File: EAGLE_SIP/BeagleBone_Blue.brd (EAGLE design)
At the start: 86.4 x 54.6 mm, 202 parts, among them J1 USD_CONNECTOR, M1 JST_ZH_2, M2 JST_ZH_2, M3 JST_ZH_2, M4 JST_ZH_2, Q3 MOSFET-N, U5 24LC_32AT-I/OT, U6 SN74LVC1G07_DCK_5, Y1 CM200C-32.768KAZF-UT, Y2 445C33D24M00000

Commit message: Small shifts
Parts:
- moved TP5 10.2 mm to (32.0, -25.1)
- moved RESET 0.15 mm to (5.17, -15.4)
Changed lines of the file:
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@@
 </element>
 <element name="RED" library="SparkFun-LED" package="LED-0603" value="RED" x="44.9199" y="-52.7939"/>
-<element name="RESET" library="SparkFun-Electromechanical" package="TACTILE-SWITCH-1101NE" value="SWITCH-MOMENTARY-2SMD-1101NE" x="5.3213" y="-15.4178" smashed="yes">
-<attribute name="PROD_ID" value="SWCH-00815" x="5.3213" y="-15.4178" size="1.778" layer="27" display="off"/>
-<attribute name="NAME" x="9.8778" y="-15.8689" size="1.27" layer="25"/>
+<element name="RESET" library="SparkFun-Electromechanical" package="TACTILE-SWITCH-1101NE" value="SWITCH-MOMENTARY-2SMD-1101NE" x="5.1689" y="-15.4178" smashed="yes">
+<attribute name="PROD_ID" value="SWCH-00815" x="5.1689" y="-15.4178" size="1.778" layer="27" display="off"/>
+<attribute name="NAME" x="9.7254" y="-15.8689" size="1.27" layer="25"/>
 </element>
 <element name="SIP" library="BeagleBone_Blue" package="OSD3358" value="OSD3358" x="46.6725" y="-36.9316" rot="MR270"/>
@@
 <attribute name="TP_SIGNAL_NAME" value="" x="65.4939" y="-11.7348" size="1.778" layer="28" rot="MR0" display="off"/>
 </element>
-<element name="TP5" library="testpad" package="B1,27" value="TPSQB1,27" x="31.8516" y="-14.9352" rot="MR0">
-<attribute name="TP_SIGNAL_NAME" value="" x="31.8516" y="-14.9352" size="1.778" layer="28" rot="MR0" display="off"/>
+<element name="TP5" library="testpad" package="B1,27" value="TPSQB1,27" x="32.004" y="-25.146" rot="MR0">
+<attribute name="TP_SIGNAL_NAME" value="" x="32.004" y="-25.146" size="1.778" layer="28" rot="MR0" display="off"/>
 </element>
 <element name="TP7" library="testpad" package="B1,27" value="TPSQB1,27" x="45.085" y="-51.0032" rot="MR180">
@@
 <wire x1="5.0391" y1="-5.334" x2="8.0391" y2="-10.134" width="0" layer="19" extent="1-1"/>
 <wire x1="2.0447" y1="-13.6784" x2="8.0391" y2="-10.134" width="0" layer="19" extent="16-16"/>
-<wire x1="2.1713" y1="-15.4178" x2="2.0447" y2="-13.6784" width="0" layer="19" extent="1-16"/>
-<wire x1="2.0447" y1="-16.4284" x2="2.1713" y2="-15.4178" width="0" layer="19" extent="1-16"/>
+<wire x1="2.0189" y1="-15.4178" x2="2.0447" y2="-13.6784" width="0" layer="19" extent="1-16"/>
+<wire x1="2.0447" y1="-16.4284" x2="2.0189" y2="-15.4178" width="0" layer="19" extent="1-16"/>
 <wire x1="2.0447" y1="-18.9284" x2="2.0447" y2="-16.4284" width="0" layer="19" extent="16-16"/>
 <wire x1="2.0189" y1="-20.5994" x2="2.0447" y2="-18.9284" width="0" layer="19" extent="1-16"/>
@@
 <wire x1="34.671" y1="-12.4079" x2="37.6809" y2="-9.4742" width="0" layer="19" extent="1-1"/>
 <wire x1="21.4353125" y1="-18.3134" x2="34.671" y2="-12.4079" width="0" layer="19" extent="1-1"/>
-<wire x1="8.4713" y1="-15.4178" x2="21.4353125" y2="-18.3134" width="0" layer="19" extent="1-1"/>
+<wire x1="8.3189" y1="-15.4178" x2="21.4353125" y2="-18.3134" width="0" layer="19" extent="1-1"/>
 <wire x1="47.3075" y1="-24.8666" x2="34.671" y2="-12.4079" width="0" layer="19" extent="1-16"/>
 </signal>
@@
 <contactref element="TP5" pad="TP"/>
 <wire x1="35.8775" y1="-28.6766" x2="52.3875" y2="-27.4066" width="0" layer="19" extent="16-16"/>
-<wire x1="31.8516" y1="-14.9352" x2="35.8775" y2="-28.6766" width="0" layer="19" extent="16-16"/>
+<wire x1="32.004" y1="-25.146" x2="35.8775" y2="-28.6766" width="0" layer="19" extent="16-16"/>
 </signal>
 <signal name="I2C0_SCL">

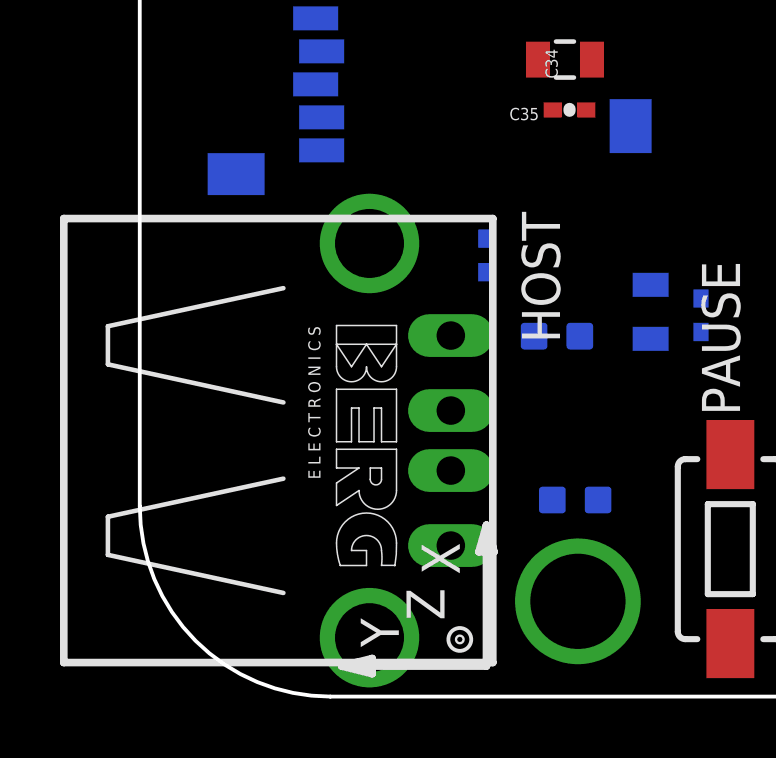
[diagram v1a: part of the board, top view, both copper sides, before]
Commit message: Small shifts for DRC
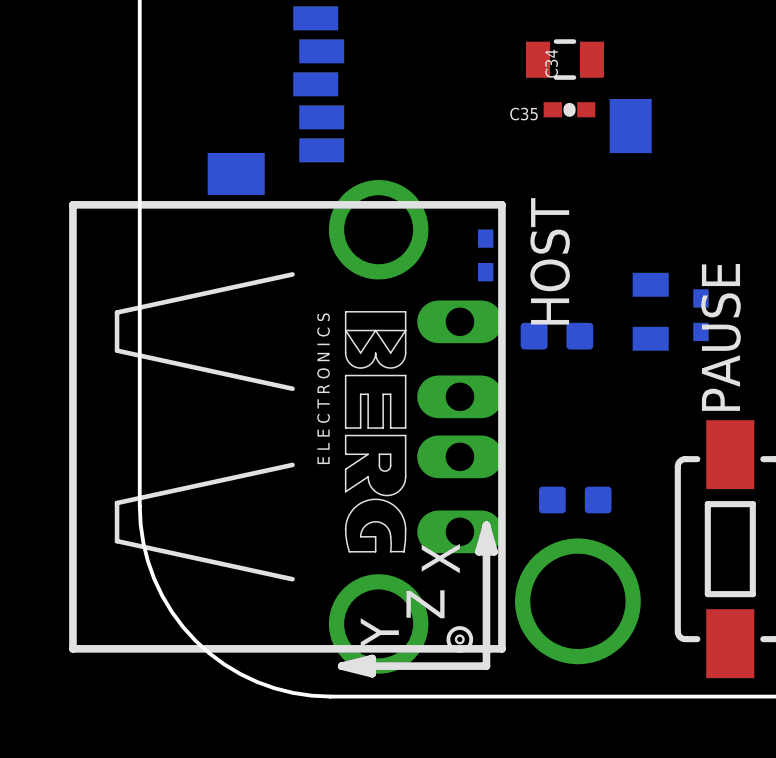
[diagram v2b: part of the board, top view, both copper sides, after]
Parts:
- moved HOST 0.55 mm to (4.41, -45.6)
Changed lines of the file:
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@@
 <element name="H1" library="SparkFun" package="SSOP24" value="TB6621FNG" x="81.0514" y="-41.3004" rot="MR90"/>
 <element name="H2" library="SparkFun" package="SSOP24" value="TB6621FNG" x="81.0387" y="-18.034" rot="MR270"/>
-<element name="HOST" library="BeagleBone_Blue" package="87520-0010BLF" value="87520-0010BLF" x="4.1021" y="-46.0756" rot="R270"/>
+<element name="HOST" library="BeagleBone_Blue" package="87520-0010BLF" value="87520-0010BLF" x="4.4069" y="-45.6184" rot="R270"/>
 <element name="I2C1" library="Strawson_Eagle_Lib" package="JST_SH_4_SMD" value="JST_SH_4" x="36.8046" y="-17.1577" smashed="yes" rot="R180">
 <attribute name="NAME" x="36.2458" y="-14.8717" size="1.016" layer="25"/>
@@
 <wire x1="18.7071" y1="-41.3385" x2="17.0307" y2="-40.883" width="0" layer="19" extent="16-16"/>
 <wire x1="11.5316" y1="-40.4622" x2="17.0307" y2="-40.883" width="0" layer="19" extent="16-16"/>
-<wire x1="7.6581" y1="-39.5056" x2="11.5316" y2="-40.4622" width="0" layer="19" extent="16-16"/>
-<wire x1="3.214" y1="-37.1928" x2="7.6581" y2="-39.5056" width="0" layer="19" extent="16-16"/>
+<wire x1="7.9629" y1="-39.0484" x2="11.5316" y2="-40.4622" width="0" layer="19" extent="16-16"/>
+<wire x1="3.214" y1="-37.1928" x2="7.9629" y2="-39.0484" width="0" layer="19" extent="16-16"/>
 <wire x1="5.864" y1="-34.2028" x2="3.214" y2="-37.1928" width="0" layer="19" extent="16-16"/>
 <wire x1="75.0189" y1="-42.7101" x2="70.4662" y2="-37.8714" width="0" layer="19" extent="1-1"/>
@@
 <wire x1="47.3075" y1="-38.8366" x2="51.1175" y2="-40.1066" width="0" layer="19" extent="16-16"/>
 <wire x1="46.9618" y1="-32.7152" x2="52.3875" y2="-35.0266" width="0" layer="19" extent="1-16"/>
-<wire x1="7.6581" y1="-52.6456" x2="15.2781" y2="-48.0568" width="0" layer="19" extent="16-16"/>
+<wire x1="7.9629" y1="-52.1884" x2="15.2781" y2="-48.0568" width="0" layer="19" extent="16-16"/>
 </signal>
 <signal name="N$6">
@@
 <contactref element="SIP" pad="R17"/>
 <contactref element="HOST" pad="3"/>
-<wire x1="38.4175" y1="-42.6466" x2="10.3681" y2="-47.0756" width="0" layer="19" extent="16-16"/>
+<wire x1="38.4175" y1="-42.6466" x2="10.6729" y2="-46.6184" width="0" layer="19" extent="16-16"/>
 </signal>
 <signal name="N$124" class="2">
 <contactref element="SIP" pad="R18"/>
 <contactref element="HOST" pad="2"/>
-<wire x1="37.1475" y1="-42.6466" x2="10.3681" y2="-45.0756" width="0" layer="19" extent="16-16"/>
+<wire x1="37.1475" y1="-42.6466" x2="10.6729" y2="-44.6184" width="0" layer="19" extent="16-16"/>
 </signal>
 <signal name="N$126">
@@
 <contactref element="L4" pad="2"/>
 <contactref element="HOST" pad="4"/>
-<wire x1="13.7541" y1="-48.0568" x2="10.3681" y2="-49.5756" width="0" layer="19" extent="16-16"/>
+<wire x1="13.7541" y1="-48.0568" x2="10.6729" y2="-49.1184" width="0" layer="19" extent="16-16"/>
 </signal>
 <signal name="N$129">
@@
 <contactref element="L5" pad="2"/>
 <contactref element="HOST" pad="1"/>
-<wire x1="13.1445" y1="-42.5958" x2="10.3681" y2="-42.5756" width="0" layer="19" extent="16-16"/>
+<wire x1="13.1445" y1="-42.5958" x2="10.6729" y2="-42.1184" width="0" layer="19" extent="16-16"/>
 </signal>
 <signal name="N$131">

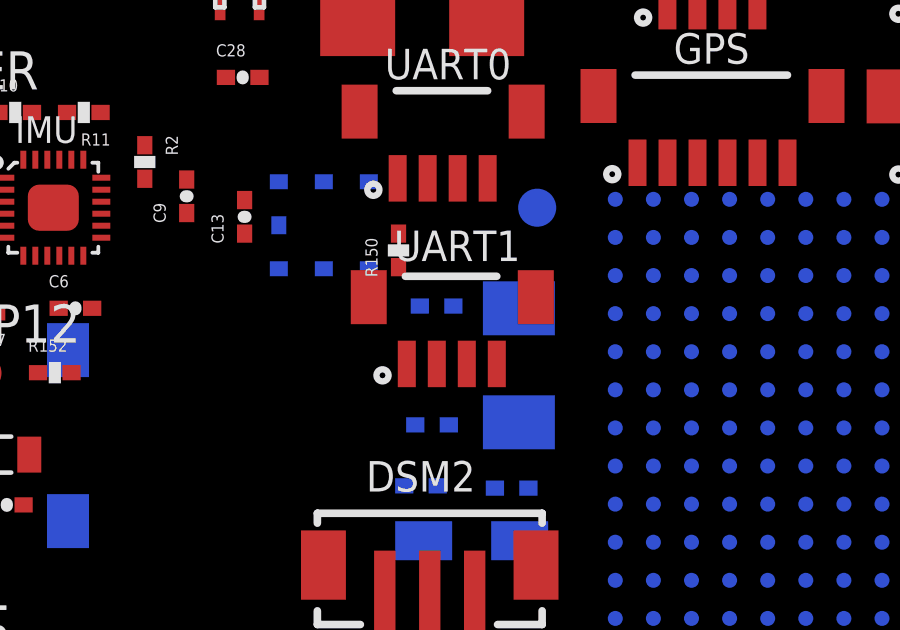
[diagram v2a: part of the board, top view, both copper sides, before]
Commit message: Switch to 2-layer OSHPark DRC
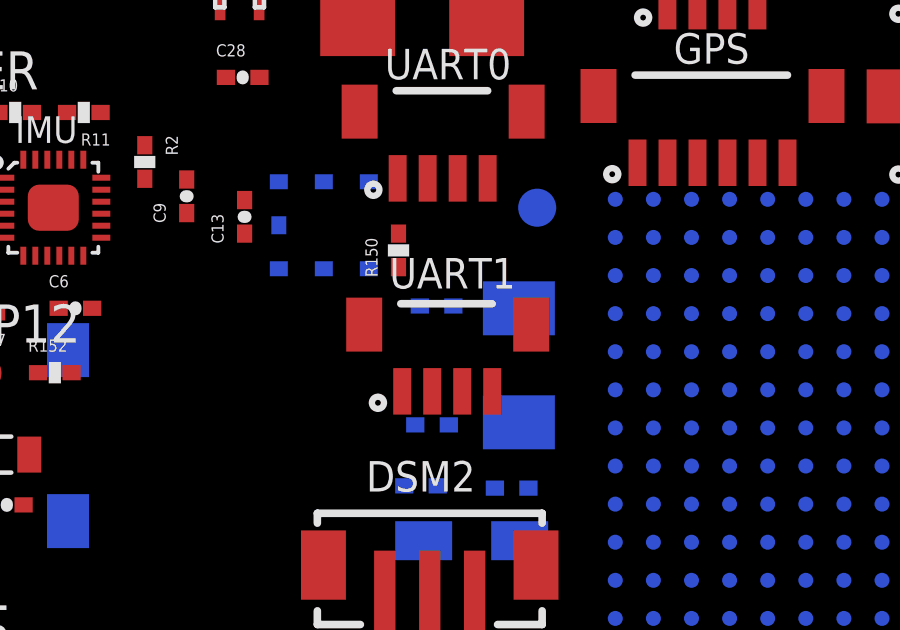
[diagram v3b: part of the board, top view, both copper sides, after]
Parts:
- moved UART1 0.93 mm to (28.0, -30.0)
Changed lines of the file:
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@@
 <layers>
 <layer number="1" name="Top" color="4" fill="1" visible="yes" active="yes"/>
-<layer number="2" name="$GND" color="1" fill="3" visible="yes" active="yes"/>
+<layer number="2" name="$GND" color="1" fill="3" visible="no" active="no"/>
 <layer number="3" name="Route3" color="4" fill="3" visible="no" active="no"/>
 <layer number="4" name="Route4" color="1" fill="4" visible="no" active="no"/>
@@
 <layer number="13" name="Route13" color="4" fill="5" visible="no" active="no"/>
 <layer number="14" name="Route14" color="1" fill="6" visible="no" active="no"/>
-<layer number="15" name="Route15" color="4" fill="6" visible="yes" active="yes"/>
+<layer number="15" name="Route15" color="4" fill="6" visible="no" active="no"/>
 <layer number="16" name="Bottom" color="1" fill="1" visible="yes" active="yes"/>
 <layer number="17" name="Pads" color="2" fill="1" visible="yes" active="yes"/>
@@
 </class>
 </classes>
-<designrules name="OSHPark-4layer">
+<designrules name="LaenPCBOrder">
 <description language="de">&lt;b&gt;EAGLE Design Rules&lt;/b&gt;
 &lt;p&gt;
@@
 &lt;p&gt;
 Please make sure your boards conform to these design rules.</description>
-<param name="layerSetup" value="(1*2*15*16)"/>
-<param name="mtCopper" value="0.035559375mm 0.01778125mm 0.0356mm 0.0356mm 0.0356mm 0.0356mm 0.0356mm 0.0356mm 0.0356mm 0.0356mm 0.0356mm 0.0356mm 0.0356mm 0.0356mm 0.01778125mm 0.035559375mm"/>
-<param name="mtIsolate" value="0.17018125mm 47mil 0.2007mm 0.1499mm 0.2007mm 0.1499mm 0.2007mm 0.1499mm 0.2007mm 0.1499mm 0.2007mm 0.1499mm 0.2007mm 0.1499mm 0.17018125mm"/>
-<param name="mdWireWire" value="5mil"/>
-<param name="mdWirePad" value="5mil"/>
-<param name="mdWireVia" value="5mil"/>
-<param name="mdPadPad" value="5mil"/>
-<param name="mdPadVia" value="5mil"/>
-<param name="mdViaVia" value="5mil"/>
-<param name="mdSmdPad" value="5mil"/>
-<param name="mdSmdVia" value="5mil"/>
-<param name="mdSmdSmd" value="5mil"/>
+<param name="layerSetup" value="(1*16)"/>
+<param name="mtCopper" value="0.0356mm 0.0356mm 0.0356mm 0.0356mm 0.0356mm 0.0356mm 0.0356mm 0.0356mm 0.0356mm 0.0356mm 0.0356mm 0.0356mm 0.0356mm 0.0356mm 0.0356mm 0.0356mm"/>
+<param name="mtIsolate" value="1.5011mm 0.1499mm 0.2007mm 0.1499mm 0.2007mm 0.1499mm 0.2007mm 0.1499mm 0.2007mm 0.1499mm 0.2007mm 0.1499mm 0.2007mm 0.1499mm 0.2007mm"/>
+<param name="mdWireWire" value="6mil"/>
+<param name="mdWirePad" value="6mil"/>
+<param name="mdWireVia" value="6mil"/>
+<param name="mdPadPad" value="6mil"/>
+<param name="mdPadVia" value="6mil"/>
+<param name="mdViaVia" value="6mil"/>
+<param name="mdSmdPad" value="6mil"/>
+<param name="mdSmdVia" value="6mil"/>
+<param name="mdSmdSmd" value="6mil"/>
 <param name="mdViaViaSameLayer" value="8mil"/>
 <param name="mnLayersViaInSmd" value="2"/>
@@
 <param name="mdDrill" value="6mil"/>
 <param name="mdSmdStop" value="0mil"/>
-<param name="msWidth" value="5mil"/>
-<param name="msDrill" value="10mil"/>
-<param name="msMicroVia" value="10mil"/>
+<param name="msWidth" value="6mil"/>
+<param name="msDrill" value="13mil"/>
+<param name="msMicroVia" value="13mil"/>
 <param name="msBlindViaRatio" value="0.5"/>
 <param name="rvPadTop" value="0.25"/>
@@
 <param name="rvMicroViaOuter" value="0.25"/>
 <param name="rvMicroViaInner" value="0.25"/>
-<param name="rlMinPadTop" value="4mil"/>
+<param name="rlMinPadTop" value="7mil"/>
 <param name="rlMaxPadTop" value="20mil"/>
-<param name="rlMinPadInner" value="4mil"/>
+<param name="rlMinPadInner" value="7mil"/>
 <param name="rlMaxPadInner" value="20mil"/>
-<param name="rlMinPadBottom" value="4mil"/>
+<param name="rlMinPadBottom" value="7mil"/>
 <param name="rlMaxPadBottom" value="20mil"/>
-<param name="rlMinViaOuter" value="4mil"/>
+<param name="rlMinViaOuter" value="7mil"/>
 <param name="rlMaxViaOuter" value="20mil"/>
-<param name="rlMinViaInner" value="4mil"/>
+<param name="rlMinViaInner" value="7mil"/>
 <param name="rlMaxViaInner" value="20mil"/>
 <param name="rlMinMicroViaOuter" value="4mil"/>
@@
 <param name="mvStopFrame" value="1"/>
 <param name="mvCreamFrame" value="0"/>
-<param name="mlMinStopFrame" value="2.5mil"/>
-<param name="mlMaxStopFrame" value="2.5mil"/>
+<param name="mlMinStopFrame" value="3mil"/>
+<param name="mlMaxStopFrame" value="3mil"/>
 <param name="mlMinCreamFrame" value="0mil"/>
 <param name="mlMaxCreamFrame" value="0mil"/>
@@
 <attribute name="NAME" x="26.924" y="-20.8661" size="1.016" layer="25"/>
 </element>
-<element name="UART1" library="Strawson_Eagle_Lib" package="JST_SH_4_SMD" value="JST_SH_4" x="28.1178" y="-29.083" smashed="yes" rot="R180">
-<attribute name="NAME" x="27.2288" y="-26.924" size="1.016" layer="25"/>
+<element name="UART1" library="Strawson_Eagle_Lib" package="JST_SH_4_SMD" value="JST_SH_4" x="27.9654" y="-29.9974" smashed="yes" rot="R180">
+<attribute name="NAME" x="27.0764" y="-27.8384" size="1.016" layer="25"/>
 </element>
 <element name="UART5" library="Strawson_Eagle_Lib" package="JST_SH_4_SMD" value="JST_SH_4" x="69.4182" y="-51.5874" smashed="yes" rot="R180">
@@
 <wire x1="14.0462" y1="-21.971" x2="14.275" y2="-24.146" width="0" layer="19" extent="1-1"/>
 <wire x1="21.6281" y1="-20.8026" x2="20.32" y2="-24.2062" width="0" layer="19" extent="1-1"/>
-<wire x1="28.6578" y1="-30.353" x2="28.353" y2="-24.1681" width="0" layer="19" extent="1-1"/>
-<wire x1="26.924" y1="-38.5572" x2="28.6578" y2="-30.353" width="0" layer="19" extent="1-1"/>
+<wire x1="28.5054" y1="-31.2674" x2="28.353" y2="-24.1681" width="0" layer="19" extent="1-1"/>
+<wire x1="26.924" y1="-38.5572" x2="28.5054" y2="-31.2674" width="0" layer="19" extent="1-1"/>
 <wire x1="34.6075" y1="-45.1866" x2="26.924" y2="-38.5572" width="0" layer="19" extent="1-16"/>
 <wire x1="34.6075" y1="-46.4566" x2="34.6075" y2="-45.1866" width="0" layer="19" extent="16-16"/>
@@
 <wire x1="27.3812" y1="-26.0096" x2="23.392" y2="-25.7302" width="0" layer="19" extent="1-16"/>
 <wire x1="27.353" y1="-24.1681" x2="27.3812" y2="-26.0096" width="0" layer="19" extent="1-1"/>
-<wire x1="27.6578" y1="-30.353" x2="27.3812" y2="-26.0096" width="0" layer="19" extent="1-1"/>
+<wire x1="27.5054" y1="-31.2674" x2="27.3812" y2="-26.0096" width="0" layer="19" extent="1-1"/>
 <wire x1="17.0307" y1="-40.883" x2="14.8844" y2="-35.052" width="0" layer="19" extent="1-16"/>
 <wire x1="18.7071" y1="-41.3385" x2="17.0307" y2="-40.883" width="0" layer="19" extent="16-16"/>
@@
 <wire x1="44.8856" y1="-23.6601" x2="40.3479" y2="-23.6474" width="0" layer="19" extent="1-1"/>
 <wire x1="44.8856" y1="-18.3007" x2="44.8856" y2="-23.6601" width="0" layer="19" extent="1-1"/>
+<wire x1="28.4226" y1="-38.5572" x2="27.5054" y2="-31.2674" width="0" layer="19" extent="1-1"/>
 <wire x1="15.2781" y1="-48.0568" x2="17.0307" y2="-40.883" width="0" layer="19" extent="16-16"/>
 <wire x1="19.685" y1="-52.8451" x2="15.2781" y2="-48.0568" width="0" layer="19" extent="1-16"/>
 <wire x1="24.7142" y1="-52.8451" x2="19.685" y2="-52.8451" width="0" layer="19" extent="1-1"/>
-<wire x1="35.8775" y1="-38.8366" x2="35.8775" y2="-46.4566" width="0" layer="19" extent="16-16"/>
+<wire x1="35.8775" y1="-38.8366" x2="28.4226" y2="-38.5572" width="0" layer="19" extent="1-16"/>
 <wire x1="35.8775" y1="-37.5666" x2="35.8775" y2="-38.8366" width="0" layer="19" extent="16-16"/>
-<wire x1="28.4226" y1="-38.5572" x2="35.8775" y2="-38.8366" width="0" layer="19" extent="1-16"/>
 <wire x1="54.9402" y1="-31.7119" x2="58.7375" y2="-24.8666" width="0" layer="19" extent="1-16"/>
 <wire x1="52.3875" y1="-35.0266" x2="54.9402" y2="-31.7119" width="0" layer="19" extent="1-16"/>
@@
 <contactref element="UART1" pad="4"/>
 <contactref element="SIP" pad="D15"/>
-<wire x1="30.6578" y1="-30.353" x2="40.9575" y2="-28.6766" width="0" layer="19" extent="1-16"/>
+<wire x1="30.5054" y1="-31.2674" x2="40.9575" y2="-28.6766" width="0" layer="19" extent="1-16"/>
 </signal>
 <signal name="UART1_RX">
 <contactref element="UART1" pad="3"/>
 <contactref element="SIP" pad="D16"/>
-<wire x1="29.6578" y1="-30.353" x2="39.6875" y2="-28.6766" width="0" layer="19" extent="1-16"/>
+<wire x1="29.5054" y1="-31.2674" x2="39.6875" y2="-28.6766" width="0" layer="19" extent="1-16"/>
 </signal>
 <signal name="MDIR_1A">

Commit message: Move parts to try to improve routing
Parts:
- moved R150 14.2 mm to (31.9, -40.0), turned to 180 degrees
- moved R16 5.21 mm to (76.3, -47.6)
- moved PWR 1.08 mm to (70.1, -35.5)

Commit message: Move parts to try to improve routing
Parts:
- moved D8 7.47 mm to (48.8, -52.7)
- moved R24 7.32 mm to (48.9, -52.8)
- moved R135 6.68 mm to (61.9, -46.1), turned to 180 degrees
- moved R29 5.09 mm to (54.4, -52.7), turned to 270 degrees
- moved D4 2.14 mm to (56.0, -52.7)
- moved D5 2.14 mm to (54.4, -52.7)
- moved D6 2.14 mm to (52.8, -52.7)
- moved E$1 2.14 mm to (53.7, -52.6)
- moved R31 2.14 mm to (56.1, -52.4)
- moved R33 2.14 mm to (52.9, -52.5)
- moved D7 2.14 mm to (51.3, -52.7)
- moved R32 2.14 mm to (51.2, -52.5)

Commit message: Move parts to try to improve routing
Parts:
- moved R21 37.5 mm to (46.7, -52.7)
- moved R127 18.8 mm to (62.0, -44.3)
- moved R24 4.12 mm to (44.8, -52.7)
- moved D8 3.81 mm to (45.0, -52.7)
- moved D10 2.44 mm to (40.6, -52.7)
- moved D11 2.44 mm to (39.0, -52.7)
- moved D12 2.44 mm to (37.5, -52.7)
- moved D13 2.44 mm to (35.9, -52.6)
- moved R62 2.44 mm to (39.1, -52.6)
- moved R61 2.44 mm to (40.7, -52.7)
- moved R63 2.44 mm to (37.5, -52.6)
- moved R64 2.44 mm to (36.0, -52.6)
- moved TP7 2.16 mm to (43.0, -51.3)
- moved GRN 2.14 mm to (48.9, -52.9)
- moved R22 2.14 mm to (48.8, -52.9)
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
